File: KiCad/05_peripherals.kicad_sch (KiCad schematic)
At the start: 0 parts

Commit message: Add SD card to scheme
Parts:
- added C400: 10uF, Capacitor_SMD:C_0603_1608Metric, symbol Device:C
- added C501: 100nF, Capacitor_SMD:C_0603_1608Metric, symbol Device:C
- added D501, D502, D503, D504, D505: PESD3V3L1BA,115, Diode_SMD:D_SOD-323, symbol Device:D_TVS
- added J501: TF-01A, esp32_s3_weather_webserver:TF01A, symbol esp32_s3_weather_webserver:TF-01A
- added R501, R502, R503, R504, R505: 10kR, Resistor_SMD:R_0805_2012Metric, symbol Device:R
- added U501: ~, symbol esp32_s3_weather_webserver:ST7735S
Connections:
- new net +3V3_PER: C400.1, C501.1, J501.4 (VDD), R501.2, R502.2, R503.2, R504.2, R505.2, U501.2 (VCC)
- new net FSPI_MISO: D501.1 (A1), J501.7 (D0/DO), R505.1
- new net FSPI_MOSI: D502.1 (A1), J501.3 (CMD/DI), R504.1
- new net FSPI_SCK: D503.1 (A1), J501.5 (CLK/SCLK), R503.1
- new net FSPI_SS: D504.1 (A1), J501.2 (D3/CS), R502.1
- new net GND: C400.2, C501.2, D501.2 (A2), D502.2 (A2), D503.2 (A2), D504.2 (A2), D505.2 (A2), J501.6 (VSS), J501.MP1, J501.MP2, J501.MP3, J501.MP4, U501.1 (GND)
- new net HSPI_MOSI: U501.4 (SDA)
- new net HSPI_SCK: U501.3 (SCL)
- new net HSPI_SS: U501.7 (CS)
- new net SD_CD: D505.1 (A1), J501.CD1, R501.1
- new net TFT_DC: U501.6 (DC)
- new net TFT_RES: U501.5 (RES)
- no-connect marks 0 -> 3
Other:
- note added: "//-------------------------- // SD SPI pins option //-------------------------- const int SD_SCK_PIN = FSPI_SCK_PIN; const int SD_MISO_PIN = FSPI_MISO_PIN; const int SD_MOSI_PIN = FSPI_MOSI_PIN; const int SD_CS_PIN = FSPI_SS_PIN; /* D3 */ //-------------------------- //-------------------------- // SD MMC pins option //-------------------------- const int SD_MMC_CLK_PIN = FSPI_SCK_PIN; // SCK OTG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"
- note added: "//-------------------------- // TFT Display //-------------------------- const int TFT_SCL_PIN = HSPI_SCK_PIN; // SPI clock signal const int TFT_SDA_PIN = HSPI_MOSI_PIN; // Serial data input pin sda const int TFT_RES_PIN = 40; // Reset pin const int TFT_DC_PIN = 41; // Data selection signal const int TFT_CS_PIN = HSPI_SS_PIN; // LCD chip select signal, for SPI protocol const int TFT_BLK_PIN = -1;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"
- note added: "SD Card"
- note added: "ST7735S"
- note added: "[5] Peripherals"

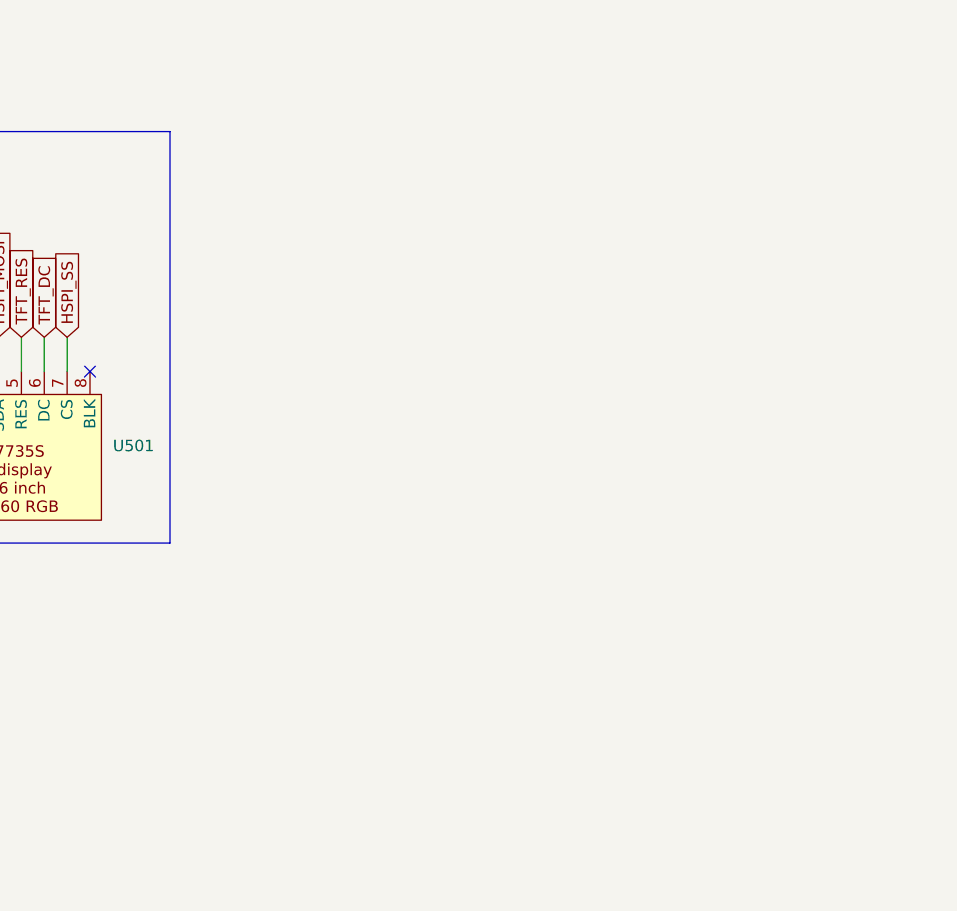
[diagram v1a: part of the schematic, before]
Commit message: Add BME280
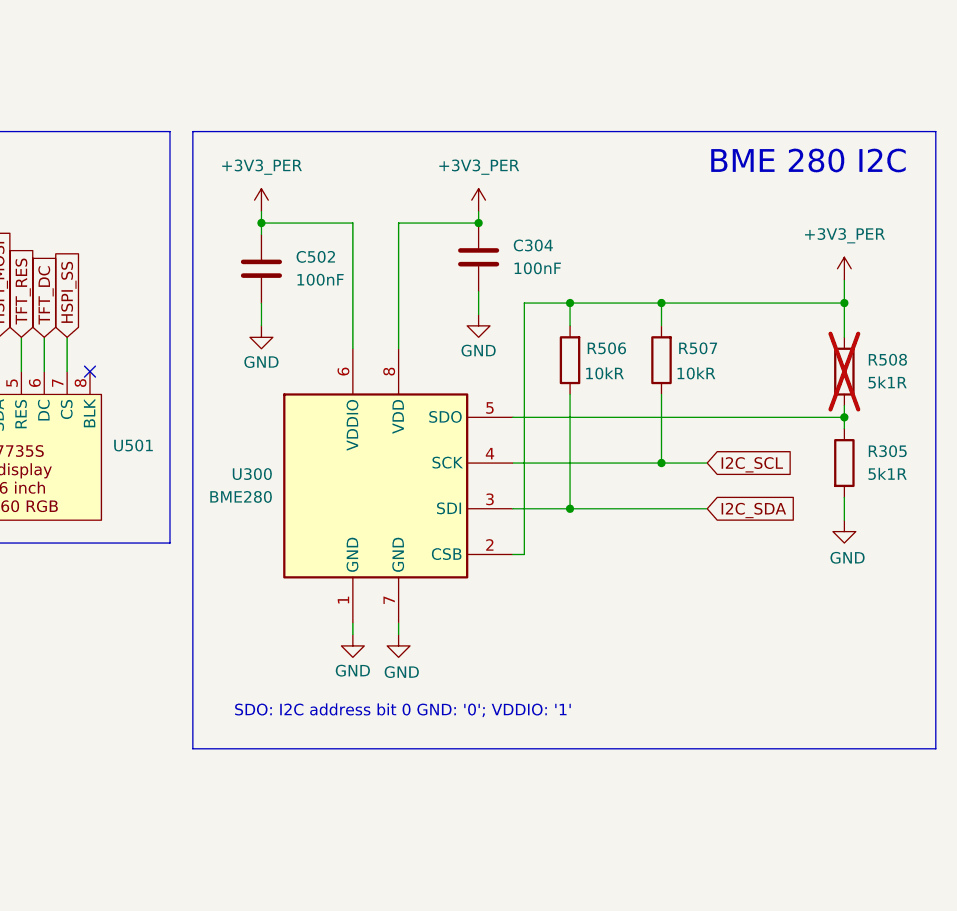
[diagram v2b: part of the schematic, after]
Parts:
- added C304, C502: 100nF, Capacitor_SMD:C_0603_1608Metric, symbol Device:C
- added R305, R508: 5k1R, Resistor_SMD:R_0805_2012Metric, symbol Device:R
- added R506, R507: 10kR, Resistor_SMD:R_0805_2012Metric, symbol Device:R
- added U300: BME280, Package_LGA:Bosch_LGA-8_2.5x2.5mm_P0.65mm_ClockwisePinNumbering, symbol Sensor:BME280
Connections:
- net +3V3_PER: now also C304.1, C502.1, R506.2, R507.2, R508.1, U300.2 (CSB), U300.6 (VDDIO), U300.8 (VDD)
- net GND: now also C304.2, C502.2, R305.2, U300.1 (GND), U300.7 (GND)
- new net: R305.1, R508.2, U300.5 (SDO)
- new net I2C_SCL: R507.1, U300.4 (SCK)
- new net I2C_SDA: R506.1, U300.3 (SDI)
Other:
- note added: "BME 280 I2C"
- note added: "SDO: I2C address bit 0 GND: '0'; VDDIO: '1'"

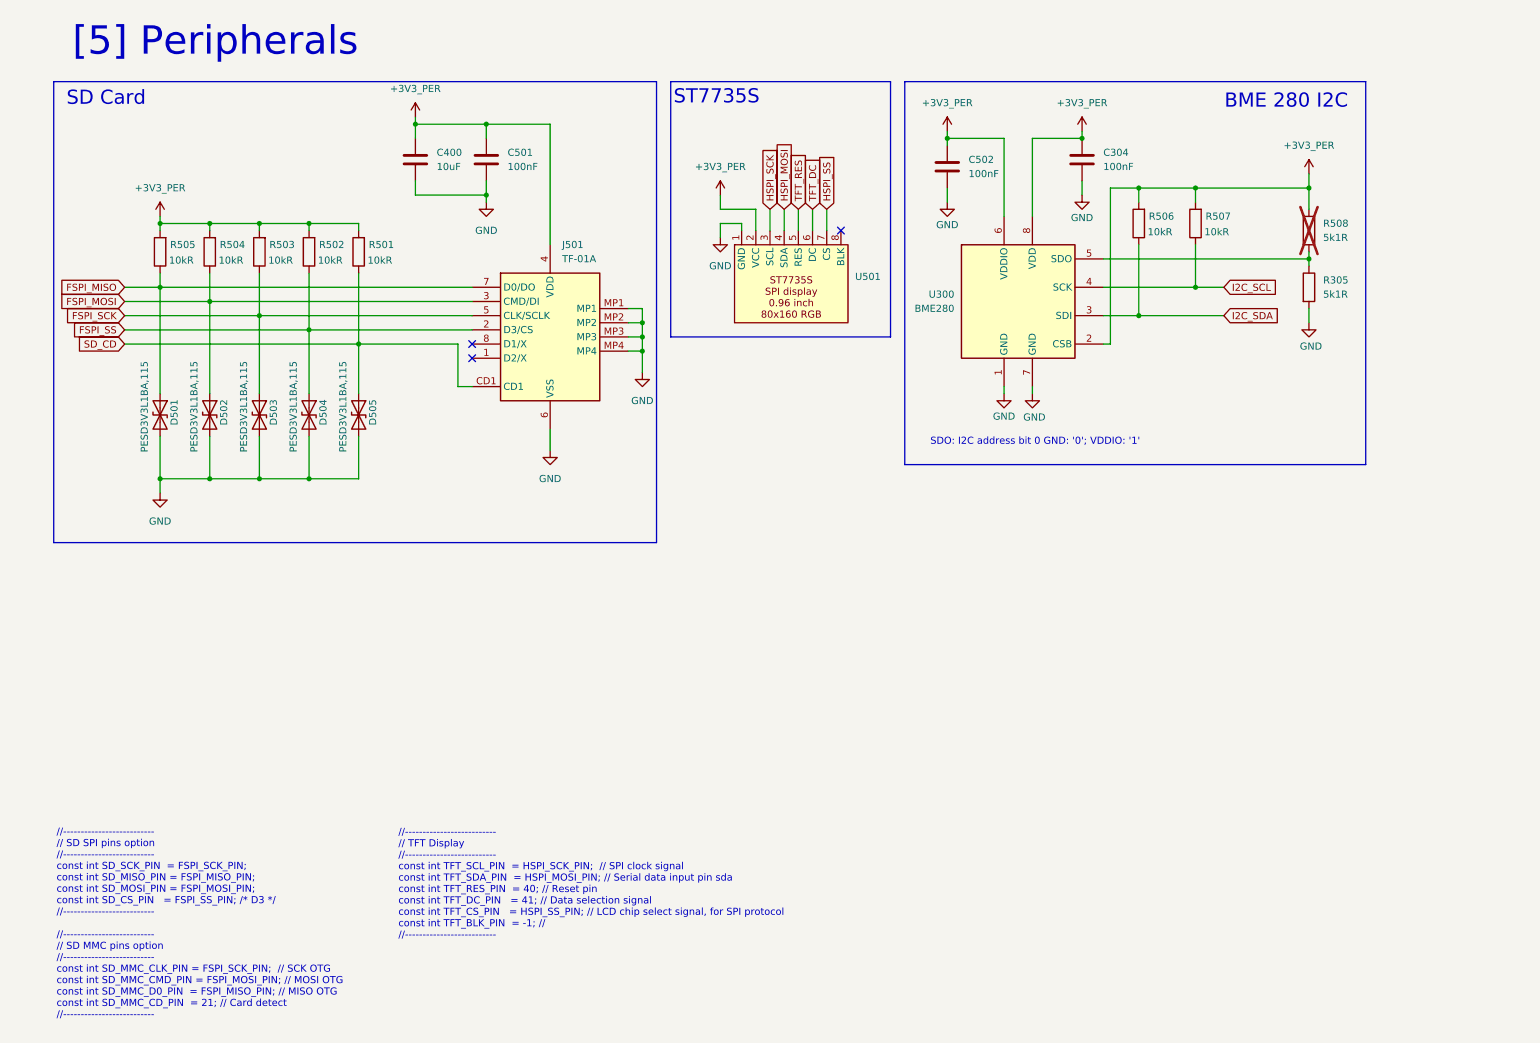
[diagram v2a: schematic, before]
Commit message: Add DS3231
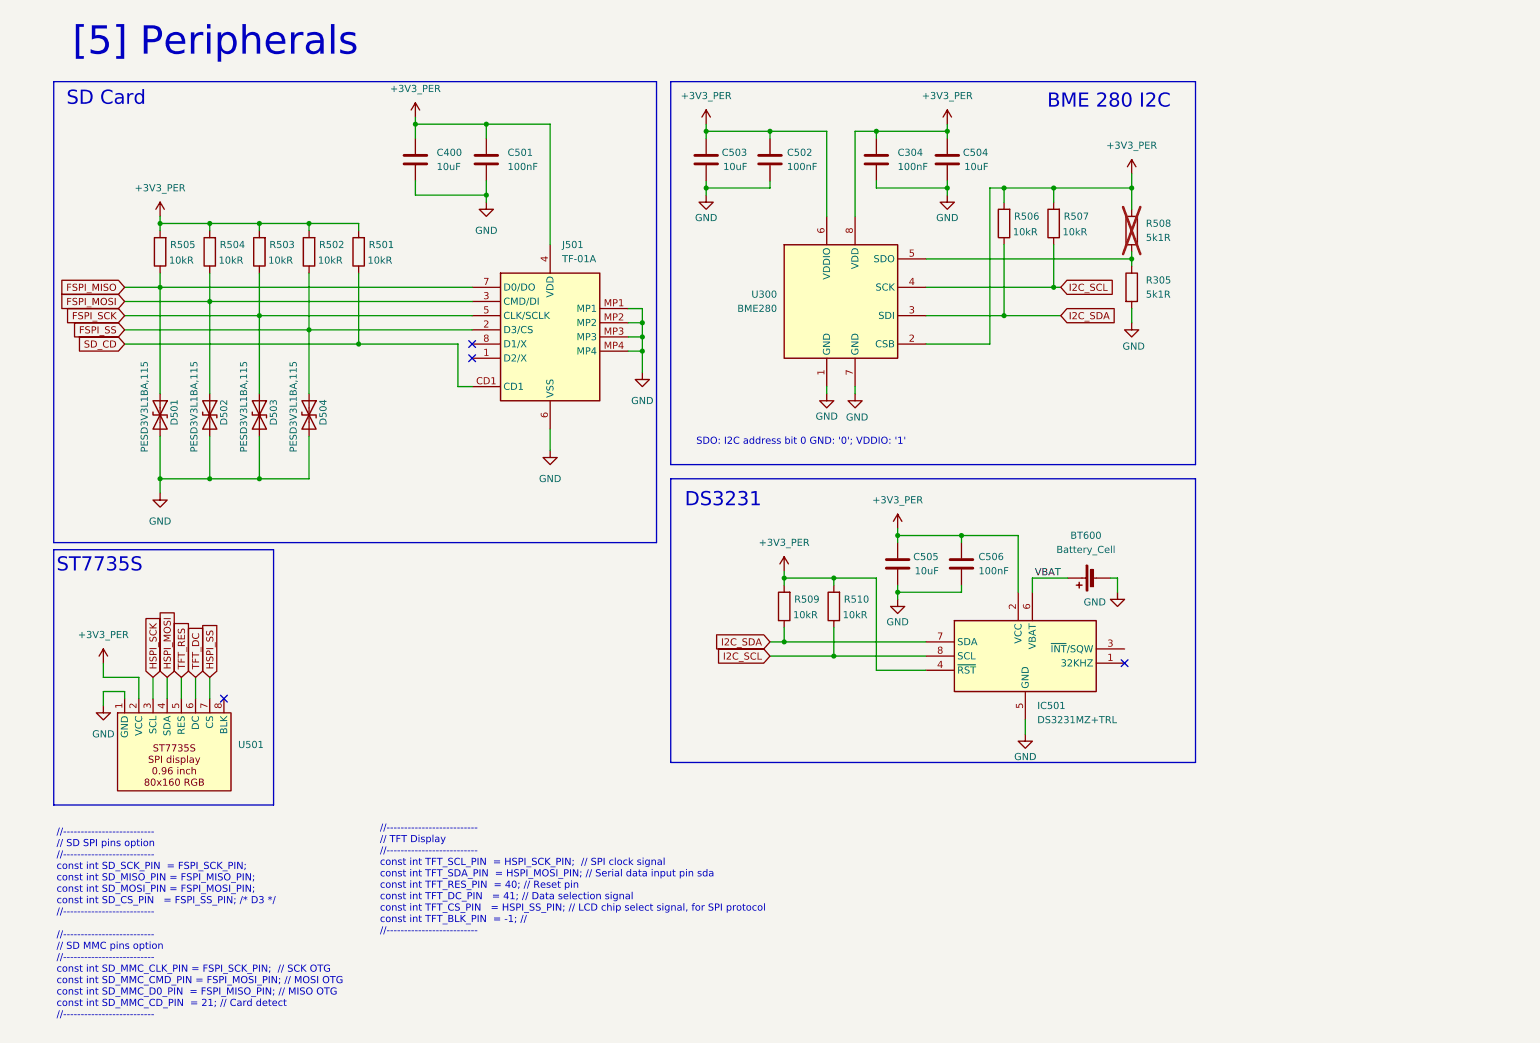
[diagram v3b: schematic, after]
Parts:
- removed D505: PESD3V3L1BA,115, Diode_SMD:D_SOD-323, symbol Device:D_TVS
- added BT600: Battery_Cell, esp32_s3_weather_webserver:CR12202, symbol Device:Battery_Cell
- added C503, C504, C505: 10uF, Capacitor_SMD:C_0603_1608Metric, symbol Device:C
- added C506: 100nF, Capacitor_SMD:C_0603_1608Metric, symbol Device:C
- added IC501: DS3231MZ+TRL, esp32_s3_weather_webserver:SOIC127P600X175-8N, symbol esp32_s3_weather_webserver:DS3231MZ+TRL
- added R509, R510: 10kR, Resistor_SMD:R_0805_2012Metric, symbol Device:R
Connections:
- net +3V3_PER: now also C503.1, C504.1, C505.1, C506.1, IC501.2 (VCC), IC501.4 (~{RST}), R509.2, R510.2
- net GND: now also BT600.2 (-), C503.2, C504.2, C505.2, C506.2, IC501.5 (GND)
- net I2C_SCL: now also IC501.8 (SCL), R510.1
- net I2C_SDA: now also IC501.7 (SDA), R509.1
- new net VBAT: BT600.1 (+), IC501.6 (VBAT)
- no-connect marks 3 -> 4
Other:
- note added: "DS3231"
- moved on the sheet: C304, C502, R305, R506, R507, R508, U300, U501

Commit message: Add analog sensors
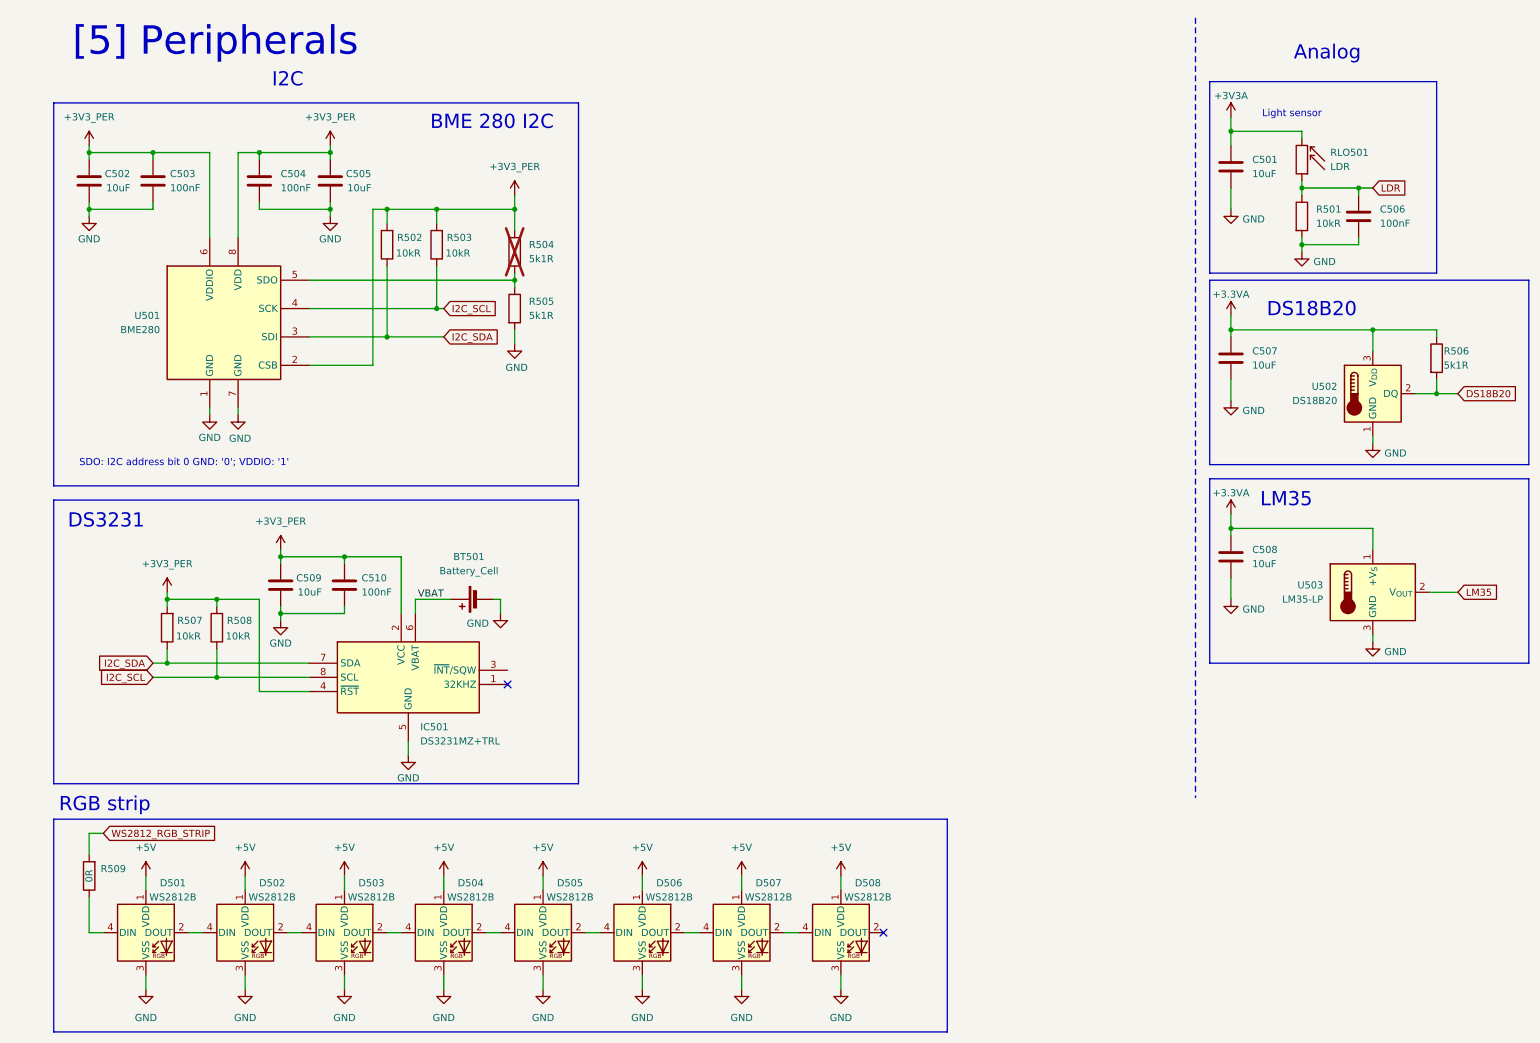
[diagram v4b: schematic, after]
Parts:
- removed C400: 10uF, Capacitor_SMD:C_0603_1608Metric, symbol Device:C
- removed D501, D502, D503, D504: PESD3V3L1BA,115, Diode_SMD:D_SOD-323, symbol Device:D_TVS
- removed J501: TF-01A, esp32_s3_weather_webserver:TF01A, symbol esp32_s3_weather_webserver:TF-01A
- removed R502, R503, R504, R505: 10kR, Resistor_SMD:R_0805_2012Metric, symbol Device:R
- removed U501: ~, symbol esp32_s3_weather_webserver:ST7735S
- added C506: 100nF, Capacitor_SMD:C_0603_1608Metric, symbol Device:C
- added C507, C508: 10uF, Capacitor_SMD:C_0805_2012Metric, symbol Device:C
- added D501, D502, D503, D504, D505, D506, D507, D508: WS2812B, LED_SMD:LED_WS2812B_PLCC4_5.0x5.0mm_P3.2mm, symbol LED:WS2812B
- added R506: 5k1R, Resistor_SMD:R_0402_1005Metric, symbol Device:R
- added R509: 0R, Resistor_SMD:R_0805_2012Metric, symbol Device:R
- added RLO501: LDR, OptoDevice:R_LDR_5.1x4.3mm_P3.4mm_Vertical, symbol Sensor_Optical:LDR07
- added U502: DS18B20, Package_TO_SOT_THT:TO-92_Inline, symbol Sensor_Temperature:DS18B20
- added U503: LM35-LP, Package_TO_SOT_THT:TO-92_Inline, symbol Sensor_Temperature:LM35-LP
- C501: value 100nF -> 10uF; footprint Capacitor_SMD:C_0603_1608Metric -> Capacitor_SMD:C_0805_2012Metric; Manufacturer Part Number CL10B104KA8NNNC -> CL21A106KOQNNNE; Manufacturer Product Number (none) -> CL21A106KOQNNNE
- R501: Manufacturer Product Number (none) -> 0805W8F1002T5E
- renumbered BT600 to BT501, C503 to C502, C502 to C503, C304 to C504, C504 to C505, C505 to C509, C506 to C510, R506 to R502, R507 to R503, R508 to R504, R305 to R505, R509 to R507, R510 to R508, U300 to U501
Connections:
- net +3V3_PER: no longer C501.1, R501.2
- net GND: now also R501.2, C506.2, C507.2, C508.2, D501.3 (VSS), D502.3 (VSS), D503.3 (VSS), D504.3 (VSS), D505.3 (VSS), D506.3 (VSS), D507.3 (VSS), D508.3 (VSS), U502.1 (GND), U503.3 (GND)
- net SD_CD renamed LDR
- net LDR: now also C506.1, RLO501.1
- new net: D507.2 (DOUT), D508.4 (DIN)
- new net: D501.2 (DOUT), D502.4 (DIN)
- new net: D501.4 (DIN), R509.1
- new net: D503.2 (DOUT), D504.4 (DIN)
- new net: D502.2 (DOUT), D503.4 (DIN)
- new net: D506.2 (DOUT), D507.4 (DIN)
- new net: D505.2 (DOUT), D506.4 (DIN)
- new net: D504.2 (DOUT), D505.4 (DIN)
- new net +3.3VA: C507.1, C508.1, R506.1, U502.3 (V_{DD}), U503.1 (+V_{S})
- new net +3V3A: C501.1, RLO501.2
- new net +5V: D501.1 (VDD), D502.1 (VDD), D503.1 (VDD), D504.1 (VDD), D505.1 (VDD), D506.1 (VDD), D507.1 (VDD), D508.1 (VDD)
- new net DS18B20: R506.2, U502.2 (DQ)
- new net LM35: U503.2 (V_{OUT})
- new net WS2812_RGB_STRIP: R509.2
- no-connect marks 4 -> 2
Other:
- note added: "Analog"
- note added: "DS18B20"
- note added: "I2C"
- note added: "LM35"
- note added: "Light sensor"
- note added: "RGB strip"
- note removed: "//-------------------------- // SD SPI pins option //-------------------------- const int SD_SCK_PIN = FSPI_SCK_PIN; const int SD_MISO_PIN = FSPI_MISO_PIN; const int SD_MOSI_PIN = FSPI_MOSI_PIN; const int SD_CS_PIN = FSPI_SS_PIN; /* D3 */ //-------------------------- //-------------------------- // SD MMC pins option //-------------------------- const int SD_MMC_CLK_PIN = FSPI_SCK_PIN; // SCK OTG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"
- note removed: "//-------------------------- // TFT Display //-------------------------- const int TFT_SCL_PIN = HSPI_SCK_PIN; // SPI clock signal const int TFT_SDA_PIN = HSPI_MOSI_PIN; // Serial data input pin sda const int TFT_RES_PIN = 40; // Reset pin const int TFT_DC_PIN = 41; // Data selection signal const int TFT_CS_PIN = HSPI_SS_PIN; // LCD chip select signal, for SPI protocol const int TFT_BLK_PIN = -1;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"
- note removed: "SD Card"
- note removed: "ST7735S"
- moved on the sheet: BT501, C502, C503, C504, C505, C509, C510, IC501, R502, R503, R504, R505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

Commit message: First scheme version
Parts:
- added C507, C513: 10uF, Capacitor_SMD:C_0603_1608Metric, symbol Device:C
- added C508, C514: 100nF, Capacitor_SMD:C_0603_1608Metric, symbol Device:C
- added IC501: VEML7700-TT, esp32_s3_weather_webserver:VEML7700, symbol esp32_s3_weather_webserver:VEML7700-TT
- added R502, R503: 10kR, Resistor_SMD:R_0805_2012Metric, symbol Device:R
- added R509: 5k1R, Resistor_SMD:R_0402_1005Metric, symbol Device:R
- added U504: DHT11, esp32_s3_weather_webserver:DHT11, symbol esp32_s3_weather_webserver:DHT11
- added U505: ~, symbol esp32_s3_weather_webserver:ENS160+AHT2x
- renumbered C505 to C502, C504 to C503, C503 to C504, C502 to C505, C507 to C509, C508 to C510, C509 to C511, C510 to C512, IC501 to IC502, R503 to R504, R502 to R505, R504 to R506, R505 to R507, R506 to R508, R507 to R510, R508 to R511, R509 to R512
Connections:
- net +3V3_PER: now also C507.1, C508.1, IC501.2 (VDD), R502.2, R503.2
- net +5V: now also C513.1, C514.1, R509.1, U504.1 (VDD), U505.1 (VIN)
- net GND: now also C507.2, C508.2, C513.2, C514.2, IC501.3 (GND), U504.4 (GND), U505.3 (GND)
- net I2C_SCL: now also IC501.1 (SCL), R502.1, U505.4 (SCL)
- net I2C_SDA: now also IC501.4 (SDA), R503.1, U505.5 (SDA)
- net DS3231_INT: now reaches IC502.3 (~{INT}/SQW)
- new net DHT11: R509.2, U504.2 (DATA)
- no-connect marks 2 -> 6
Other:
- note added: "Air quality sensor"
- note added: "DHT11"
- note added: "ENS160+AHT2x"
- note added: "Real Time Clock"
- note added: "Temperature Humidity Pressure Sensor"
- note added: "Temperature Humidity Sensor"
- note added: "VEML 7700"
- moved on the sheet: BT501, C502, C503, C504, C505, C511, C512, IC502, R504, R505, R506, R507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
